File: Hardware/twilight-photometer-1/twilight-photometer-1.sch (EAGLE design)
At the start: 9 parts, among them U1 TLC271BIDR

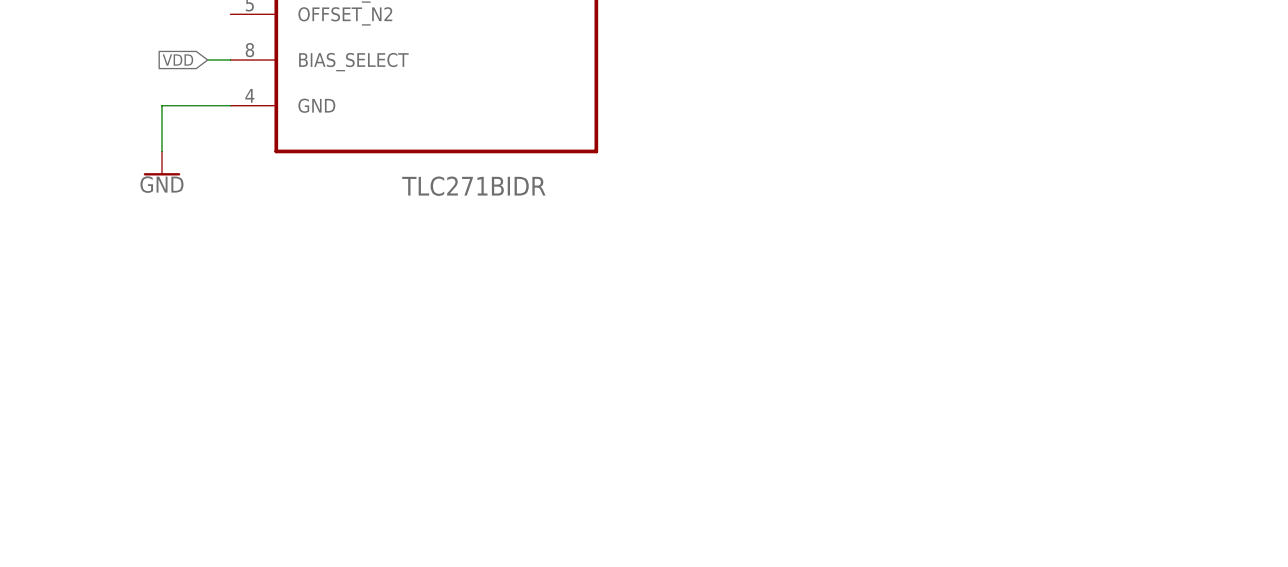
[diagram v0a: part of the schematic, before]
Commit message: Partial board layout
Still need to finish circut schematic
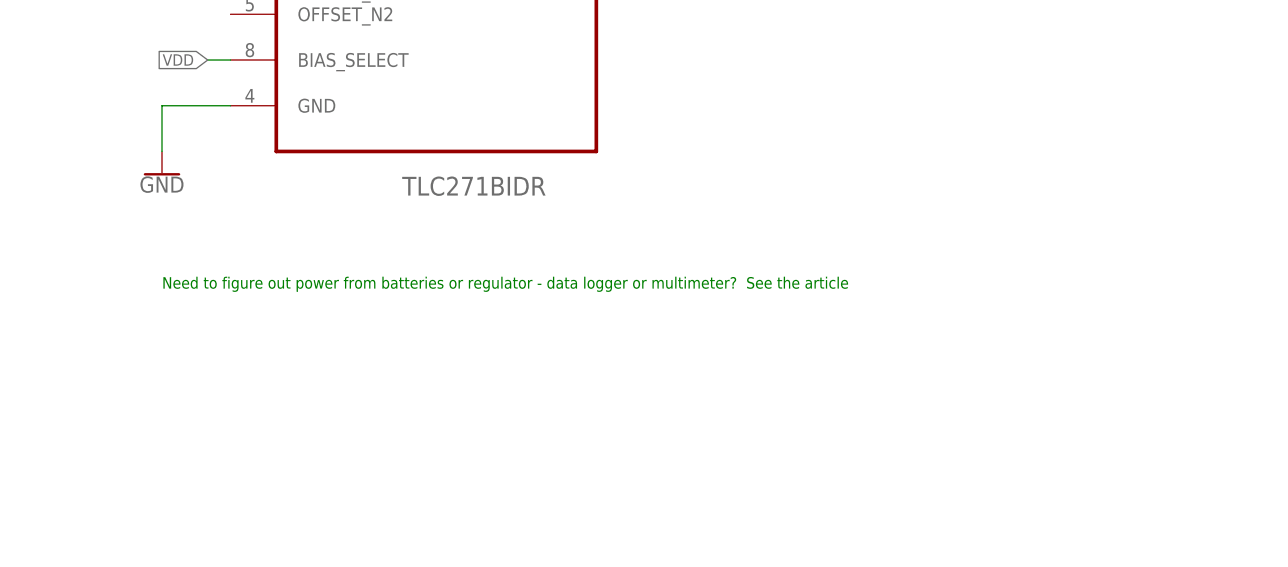
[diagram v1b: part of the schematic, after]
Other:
- note added: "Need to figure out power from batteries or regulator - data logger or multimeter? See the article"
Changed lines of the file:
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@@
 <sheet>
 <plain>
+<text x="81.28" y="71.12" size="1.27" layer="91">Need to figure out power from batteries or regulator - data logger or multimeter?  See the article</text>
 </plain>
 <instances>

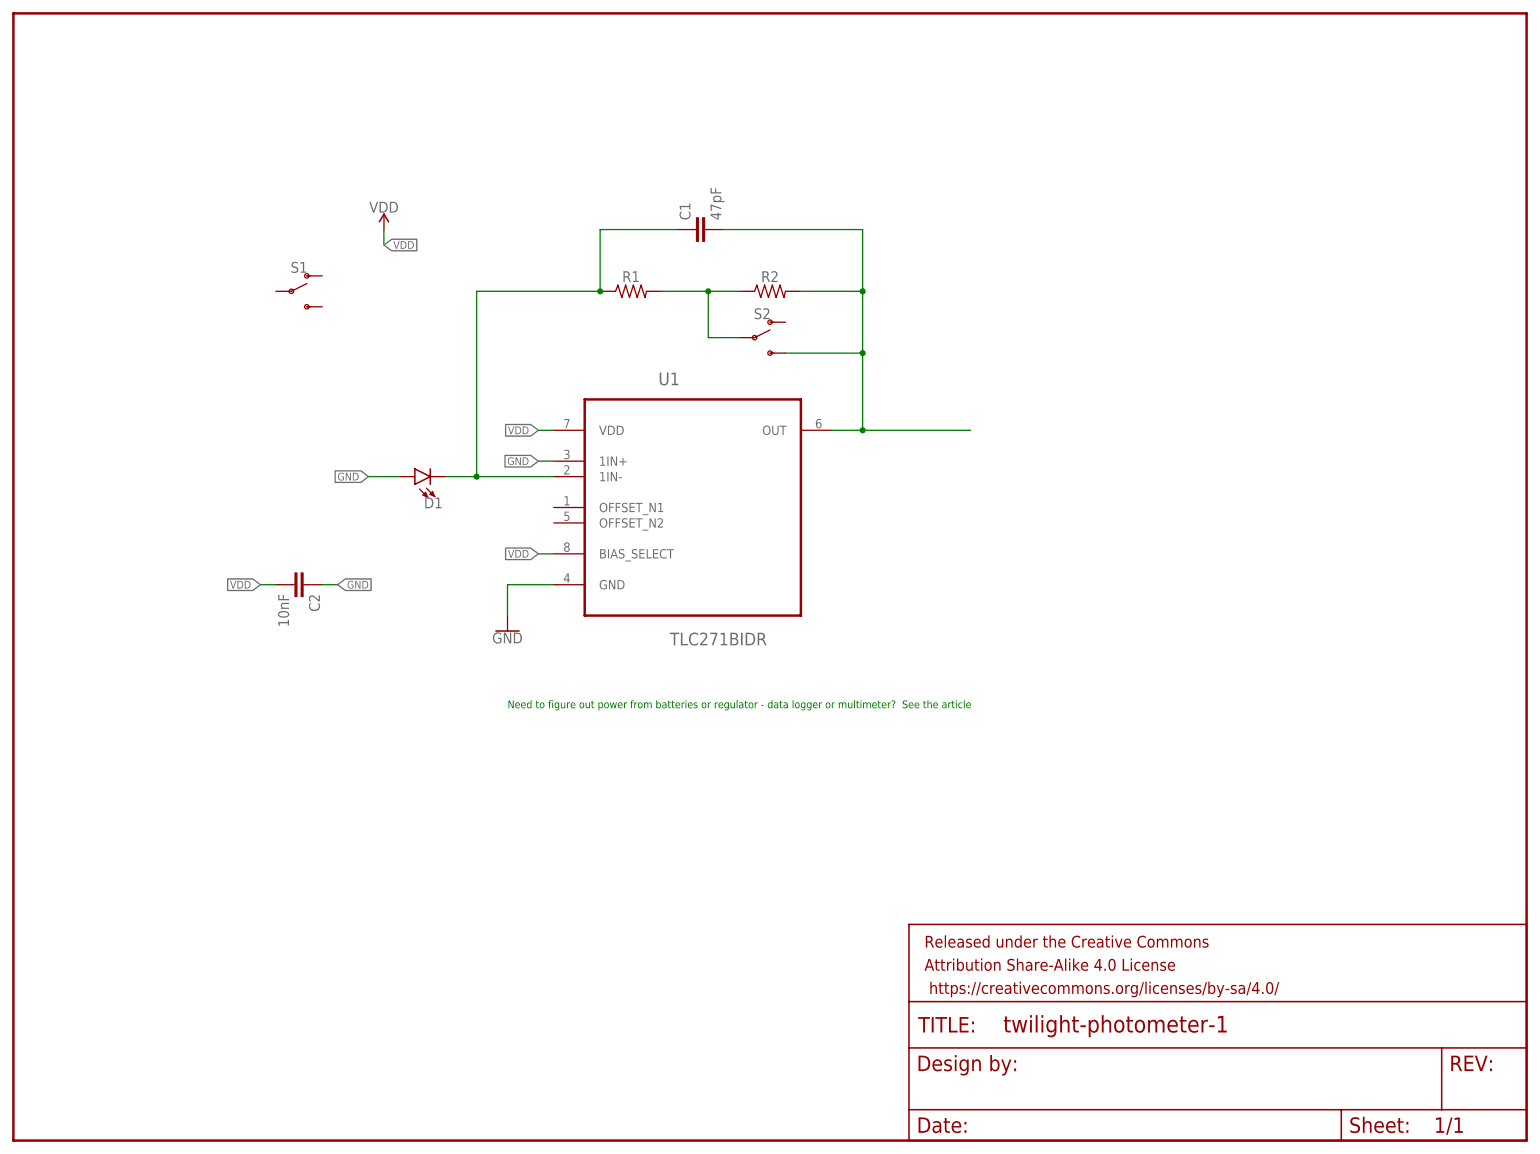
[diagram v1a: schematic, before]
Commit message: Finished routing, Board sizing for V1
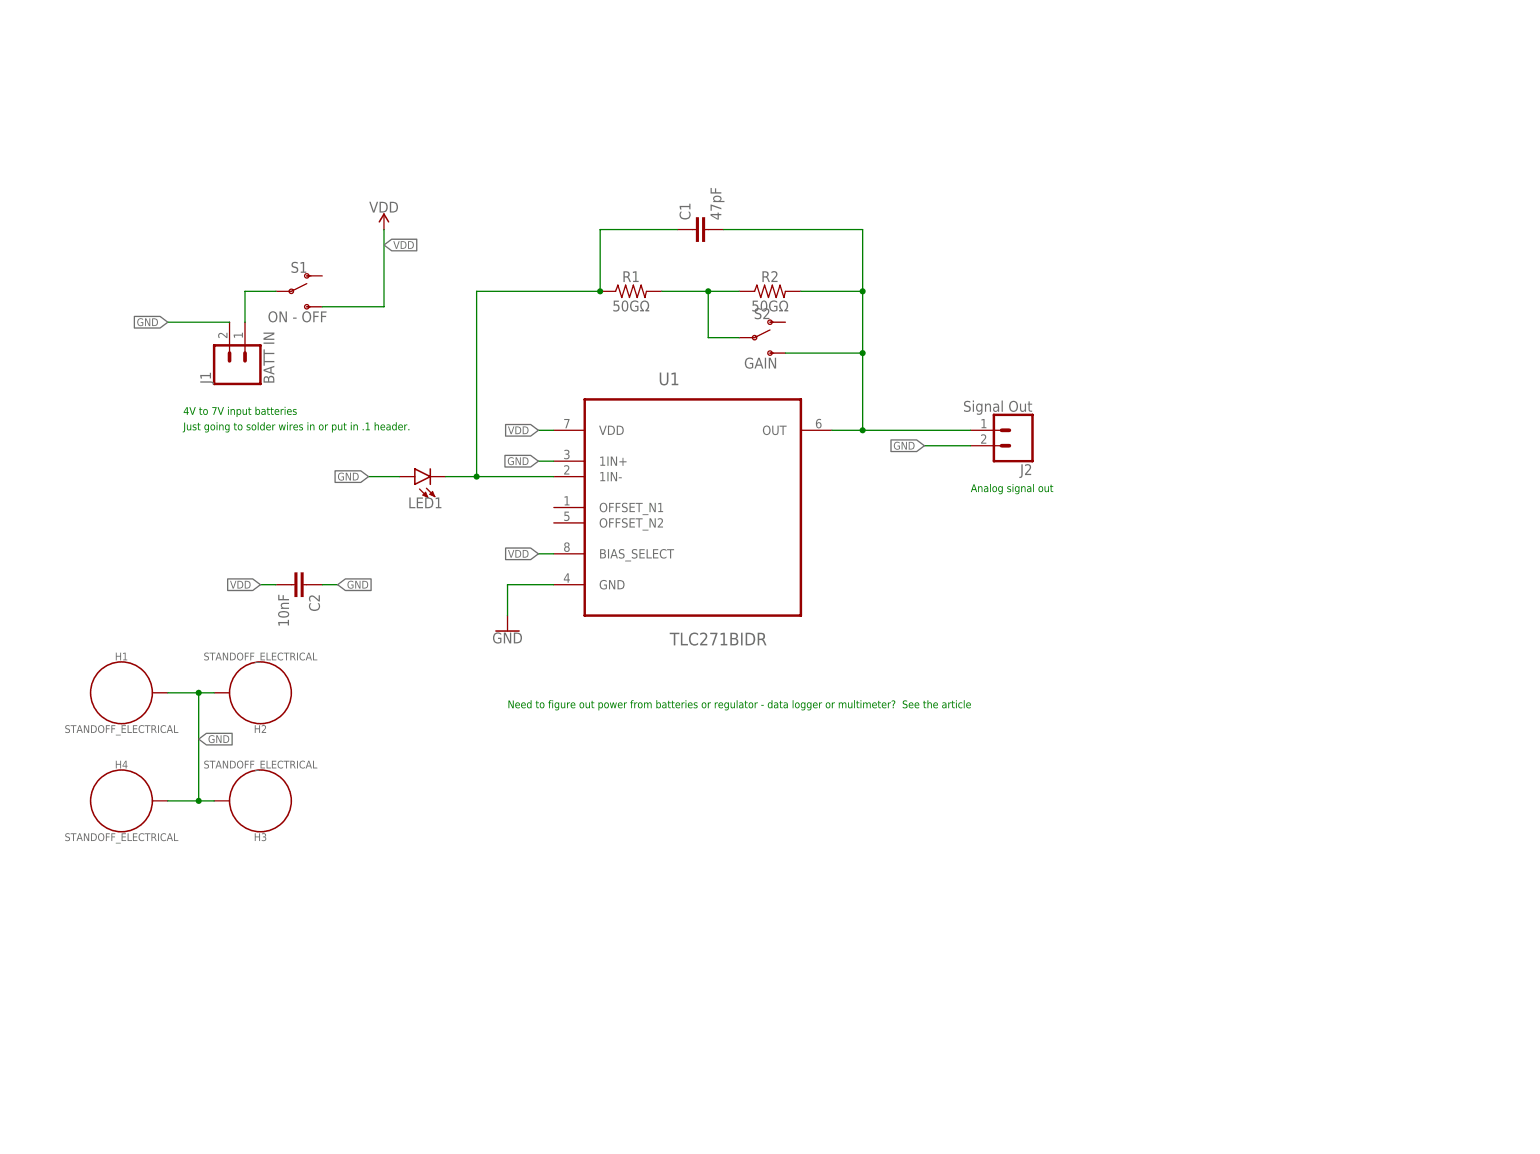
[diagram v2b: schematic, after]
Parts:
- removed FRAME1: FRAME-LETTER, SparkFun-Aesthetics:FRAME-LETTER
- added H1, H2, H3, H4: STANDOFF_ELECTRICAL, SparkFun-Hardware:STANDOFF_ELECTRICAL
- added J1: BATT IN, SparkFun-Connectors:CONN_02LOCK_LONGPADS
- added J2: Signal Out, SparkFun-Connectors:CONN_02LOCK_LONGPADS
- R1, R2: value (none) -> 50GΩ
- S1: value (none) -> ON - OFF
- S2: value (none) -> GAIN
- renumbered D1 to LED1
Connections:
- new net N$3: J1.1, S1.P
- net GND: now also H1.P$1, H2.P$1, H3.P$1, H4.P$1, J1.2, J2.2
- net N$5: now also J2.1
- net VDD: now also S1.S
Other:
- note added: "4V to 7V input batteries"
- note added: "Analog signal out"
- note added: "Just going to solder wires in or put in .1 header."
